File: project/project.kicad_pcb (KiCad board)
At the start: 4 copper layers, 164 x 254 mm, 174 parts

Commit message: adding more things
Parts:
- removed Cs19, Cs20: chair s, -local:chair_small
- removed the R83 at (128.0, 275.0)
- added R12: Painting table, -local:_o_painting_table__, F.Cu at (179.0, 29.0)
- added R20: palet rack2, -local:_o_palet_rack__, F.Cu at (123.0, 115.0)
- added R21: Broken tools, -local:_o_broken_tools_shelf__, F.Cu at (98.5, 58.0)
- added R22: Strings and wheels, -local:_o_strings_wheels_shelf__, F.Cu at (80.0, 68.5)
- added R39: cube container, -local:_o_cube_container__, F.Cu at (93.0, 86.0)
- added R45: Trash el, -local:_o_trash_electronics__, F.Cu at (99.5, 76.0)
- added R55: Dirty small table, -local:_o_dirty_small_table__, F.Cu at (179.2, 145.5)
- added R58: Presentation chairs, -local:_o_chair_box__, F.Cu at (56.0, 206.0)
- added R65: Lightbox, -local:_e_lightbox__, F.Cu at (136.0, 244.0)
- added R80: el center shitty table, -local:_e_shitty_table__, F.Cu at (102.2, 189.5)
- R19: renamed from R35; value palet rack -> palet rack1
- R68: renamed from R78; footprint -local:_e_kitchen_table2__ -> -local:_e_shitty_table__
- R73: renamed from R69; footprint -local:_e_lab_table_x3__ -> -local:_e_lab_table_normal__
- R74: renamed from R70; footprint -local:_e_lab_table_x3__ -> -local:_e_lab_table_tall__
- R75: renamed from R71; footprint -local:_e_lab_table_x3__ -> -local:_e_lab_table_tall__
- R78: renamed from R74; footprint -local:_e_center_table2__ -> -local:_e_center_table1__
- R99: renamed from R90; footprint -local:_o_rack__ -> -local:_e_rack__
- moved R19 38.1 mm to (123.0, 86.0)
- moved R31 10.7 mm to (144.2, 114.3)
- moved Be7 10.0 mm to (128.8, 231.5)
- moved R99 9.62 mm to (79.5, 186.0), turned to 90 degrees
- moved R53 3.61 mm to (161.0, 143.0)
- moved R54 3.61 mm to (179.0, 142.7)
- moved R57 3.00 mm to (80.0, 226.0)
- moved Cb17 2.83 mm to (178.0, 199.0)
- moved Cb18 2.24 mm to (92.0, 211.0)
- moved Cb3 2.00 mm to (178.0, 209.0)
- moved R72 1.75 mm to (97.8, 235.0)
- moved R7 1.25 mm to (117.8, 25.5)
- moved R6 1.12 mm to (139.0, 55.0)
- renumbered R12 to R13, R13 to R14, R14 to R17, R36 to R18, R19 to R23, R20 to R24, R21 to R25, R22 to R26, R23 to R27, R24 to R28, R25 to R29, R26 to R30, R27 to R31, R28 to R32, R29 to R33, R30 to R34, R31 to R35, R32 to R36, R33 to R37, R34 to R38, R37 to R40, R38 to R41, R39 to R42, R40 to R43, R41 to R44, R42 to R46, R43 to R47, R44 to R48, R45 to R49, R46 to R50, R47 to R51, R48 to R52, R18 to R53, R17 to R54, R49 to R56, R50 to R57, R51 to R59, R52 to R60, R53 to R61, R54 to R62, R55 to R63, R56 to R64, R76 to R66, R77 to R67, R79 to R69, R80 to R70, R81 to R71, R82 to R72, R72 to R76, R73 to R77, R75 to R79, R57 to R81, R58 to R82, R59 to R83, R60 to R84, R61 to R85, R62 to R86, R63 to R87, R64 to R88, R65 to R89, R66 to R90, R67 to R91, R68 to R92, R84 to R93, R85 to R94, R86 to R95, R87 to R96, R88 to R97, R89 to R98
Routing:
- net (no net): track 682.5 -> 683.3 mm

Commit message: moving things around
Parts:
- removed Be8: bench, -local:_e_bench__
- removed the R34 at (164.5, 173.6)
- removed the R38 at (185.5, 173.6)
- removed the R64 at (103.0, 178.0)
- removed the R92 at (203.0, 227.8)
- added R33: clamps, -local:_o_clamps__, F.Cu at (150.0, 116.5)
- added R35: cube container, -local:_o_cube_container_x2__, F.Cu at (107.0, 87.0)
- added R39: palet rack, -local:_o_palet_rack_x4__, F.Cu at (106.5, 58.0)
- added R40: palet rack, -local:_o_palet_rack_x4__, F.Cu at (159.5, 86.0)
- added R44: shitty table, -local:_o_shitty_table_x4__, F.Cu at (203.2, 72.5)
- added R47: trash bucket, -local:_o_trash_bucket_x2__, F.Cu at (188.0, 174.0)
- added R5: cnc router, -local:_o_cnc_mill__, F.Cu at (136.5, 47.5)
- Be1, Be2, Be3, Be4, Be5, Be6, Be7: footprint -local:_e_bench__ -> -local:_e_bench_x7__
- R14: renamed from R13; footprint -local:_o_thin_shelf__ -> -local:_o_thin_shelf_single__
- R19: renamed from R23; footprint -local:_o_wheel_tower2__ -> -local:_o_wheel_tower2_x7__
- R29: renamed from R33; footprint -local:_o_thin_shelf__ -> -local:_o_thin_shelf_x2__
- R3: footprint -local:_o_wheel_tower2__ -> -local:_o_wheel_tower2_x7__
- R30: renamed from R35; footprint -local:_o_thin_shelf__ -> -local:_o_thin_shelf_x2__
- R31: renamed from R37; value ppe -> ppe and files
- R32: renamed from R36; footprint -local:_o_thin_shelf__ -> -local:_o_thin_shelf_single__
- R34: renamed from R39; footprint -local:_o_cube_container__ -> -local:_o_cube_container_x2__
- R37: renamed from R19; value palet rack1 -> palet rack; footprint -local:_o_palet_rack__ -> -local:_o_palet_rack_x4__
- R38: renamed from R20; value palet rack2 -> palet rack; footprint -local:_o_palet_rack__ -> -local:_o_palet_rack_x4__
- R43: value trash bottles -> shitty table; footprint -local:_o_trash_bottles__ -> -local:_o_shitty_table_x4__
- R46: renamed from R41; footprint -local:_o_trash_bucket__ -> -local:_o_trash_bucket_x2__
- R51: renamed from R46; footprint -local:_o_wheel_tower1__ -> -local:_o_wheel_tower1_x7__
- R52: renamed from R47; footprint -local:_o_wheel_tower1__ -> -local:_o_wheel_tower1_x7__
- R53: renamed from R48; footprint -local:_o_wheel_tower1__ -> -local:_o_wheel_tower1_x7__
- R54: renamed from R49; footprint -local:_o_wheel_tower1__ -> -local:_o_wheel_tower1_x7__
- R55: renamed from R50; footprint -local:_o_wheel_tower1__ -> -local:_o_wheel_tower1_x7__
- R56: renamed from R51; footprint -local:_o_wheel_tower1__ -> -local:_o_wheel_tower1_x7__
- R57: renamed from R52; footprint -local:_o_wheel_tower1__ -> -local:_o_wheel_tower1_x7__
- R72: renamed from R68; footprint -local:_e_shitty_table__ -> -local:_o_shitty_table_x4__
- R78: renamed from R74; footprint -local:_e_lab_table_tall__ -> -local:_e_lab_table_tall_x2__
- R79: renamed from R75; footprint -local:_e_lab_table_tall__ -> -local:_e_lab_table_tall_x2__
- R80: renamed from R76; footprint -local:_e_center_table1__ -> -local:_e_center_table1_x3__
- R81: renamed from R77; footprint -local:_e_center_table1__ -> -local:_e_center_table1_x3__
- R82: renamed from R78; footprint -local:_e_center_table1__ -> -local:_e_center_table1_x3__
- R84: renamed from R80; footprint -local:_e_shitty_table__ -> -local:_o_shitty_table_x4__
- R85: renamed from R81; footprint -local:_o_wheel_tower2__ -> -local:_o_wheel_tower2_x7__
- R86: renamed from R82; footprint -local:_o_wheel_tower2__ -> -local:_o_wheel_tower2_x7__
- R87: renamed from R83; footprint -local:_o_wheel_tower2__ -> -local:_o_wheel_tower2_x7__
- R88: renamed from R84; footprint -local:_o_wheel_tower2__ -> -local:_o_wheel_tower2_x7__
- R89: renamed from R85; footprint -local:_o_wheel_tower2__ -> -local:_o_wheel_tower2_x7__
- R90: renamed from R86; footprint -local:_o_wheel_tower2__ -> -local:_o_wheel_tower2_x7__
- R91: renamed from R87; value el1 t -> el; footprint -local:_o_wheel_tower3__ -> -local:_o_wheel_tower3_x5__
- R92: renamed from R88; value el2 t -> el; footprint -local:_o_wheel_tower3__ -> -local:_o_wheel_tower3_x5__
- R93: renamed from R89; value el3 t -> el; footprint -local:_o_wheel_tower3__ -> -local:_o_wheel_tower3_x5__
- R94: renamed from R90; value el4 t -> el; footprint -local:_o_wheel_tower3__ -> -local:_o_wheel_tower3_x5__
- R95: renamed from R91; value el5 t -> el; footprint -local:_o_wheel_tower3__ -> -local:_o_wheel_tower3_x5__
- moved R43 239.7 mm to (106.5, 55.2), turned to 180 degrees
- moved R46 118.8 mm to (80.0, 130.0), turned to 90 degrees
- moved R50 97.8 mm to (107.0, 173.5), turned to 180 degrees
- moved R49 93.3 mm to (203.0, 118.0), turned to -90 degrees
- moved R90 81.1 mm to (203.0, 228.8), turned to -90 degrees
- moved R48 68.0 mm to (187.0, 117.0), turned to -90 degrees
- moved R28 65.8 mm to (203.2, 101.8), turned to -90 degrees
- moved R84 62.3 mm to (143.5, 142.8), turned to 0 degrees
- moved R24 60.2 mm to (124.0, 115.5), turned to 0 degrees
- moved R76 58.4 mm to (93.2, 176.8), turned to 0 degrees
- moved R23 57.0 mm to (150.2, 57.8), turned to 0 degrees
- moved R60 56.8 mm to (122.5, 143.2), turned to 0 degrees
- moved R8 55.1 mm to (164.2, 55.0), turned to 180 degrees
- moved R59 53.1 mm to (183.0, 89.8)
- moved R17 43.7 mm to (180.5, 142.5), turned to 180 degrees
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- renumbered R9 to R10, R97 to R100, R98 to R101, R99 to R102, R10 to R11, R11 to R12, R12 to R13, R14 to R15, R15 to R16, R16 to R17, R17 to R18, R24 to R20, R25 to R21, R26 to R22, R27 to R23, R28 to R24, R29 to R25, R30 to R26, R31 to R27, R32 to R28, R18 to R36, R21 to R41, R22 to R42, R40 to R45, R42 to R48, R44 to R49, R45 to R50, R53 to R58, R54 to R59, R5 to R6, R55 to R60, R56 to R61, R57 to R62, R58 to R63, R59 to R64, R60 to R65, R61 to R66, R62 to R67, R63 to R68, R65 to R69, R6 to R7, R66 to R70, R67 to R71, R69 to R73, R70 to R74, R71 to R75, R72 to R76, R73 to R77, R7 to R8, R79 to R83, R8 to R9, R93 to R96, R94 to R97, R95 to R98, R96 to R99
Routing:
- net Net-(L1-Pad1): track 1827.7 -> 1941.7 mm
- net (no net): track 683.3 -> 716.4 mm
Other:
- copper layers 4 -> 6
- board text added: "needs: * 1f 4A"
- board text added: "needs: * 3f 4A"

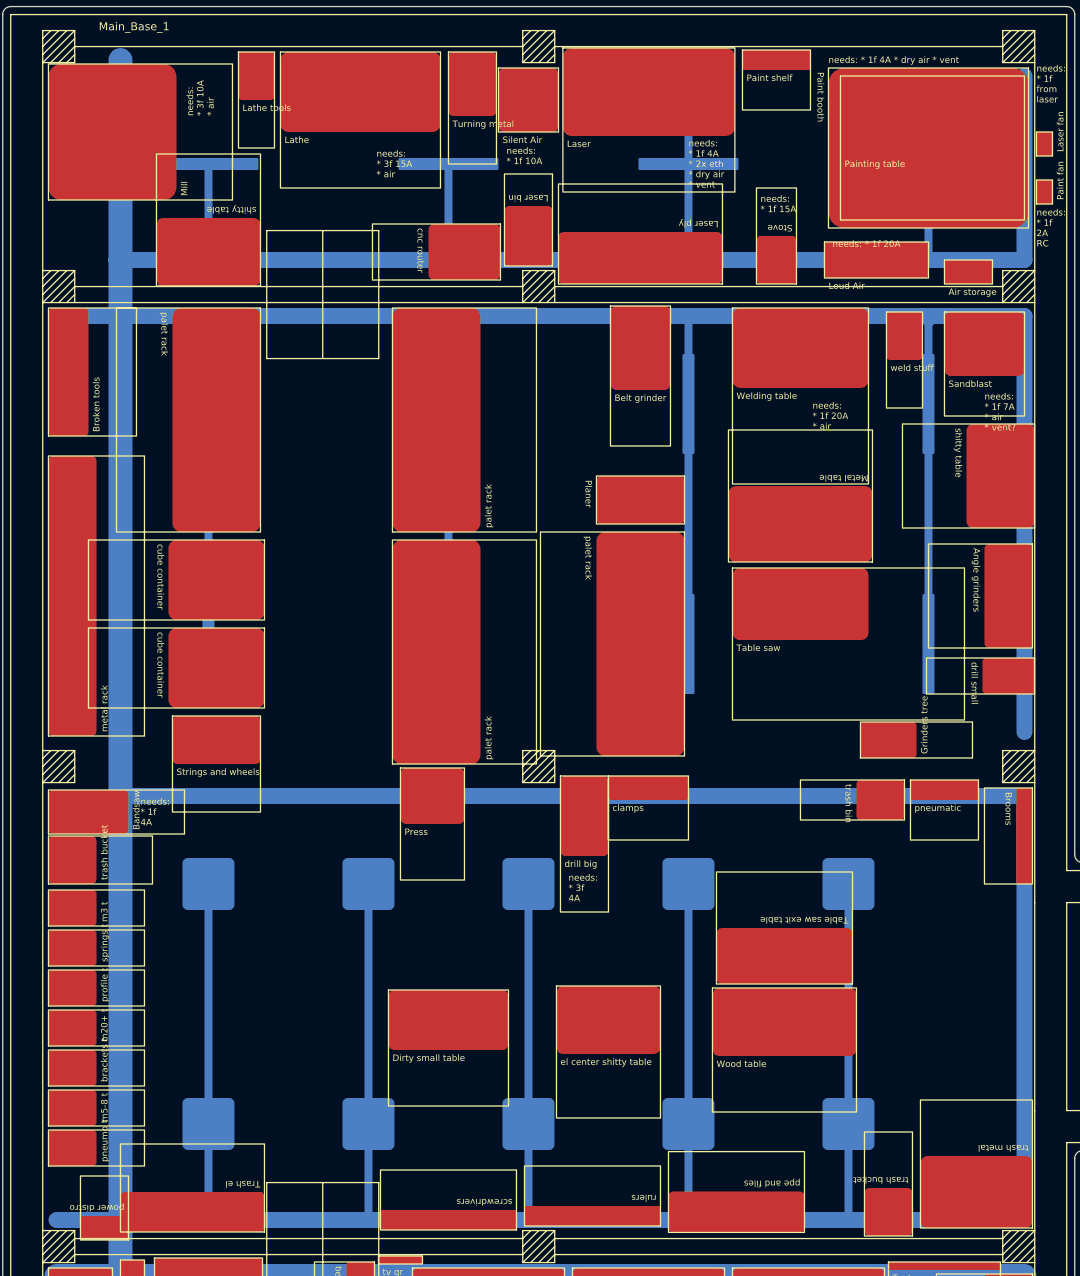
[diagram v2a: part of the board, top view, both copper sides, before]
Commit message: adding light and moving electrical stuff
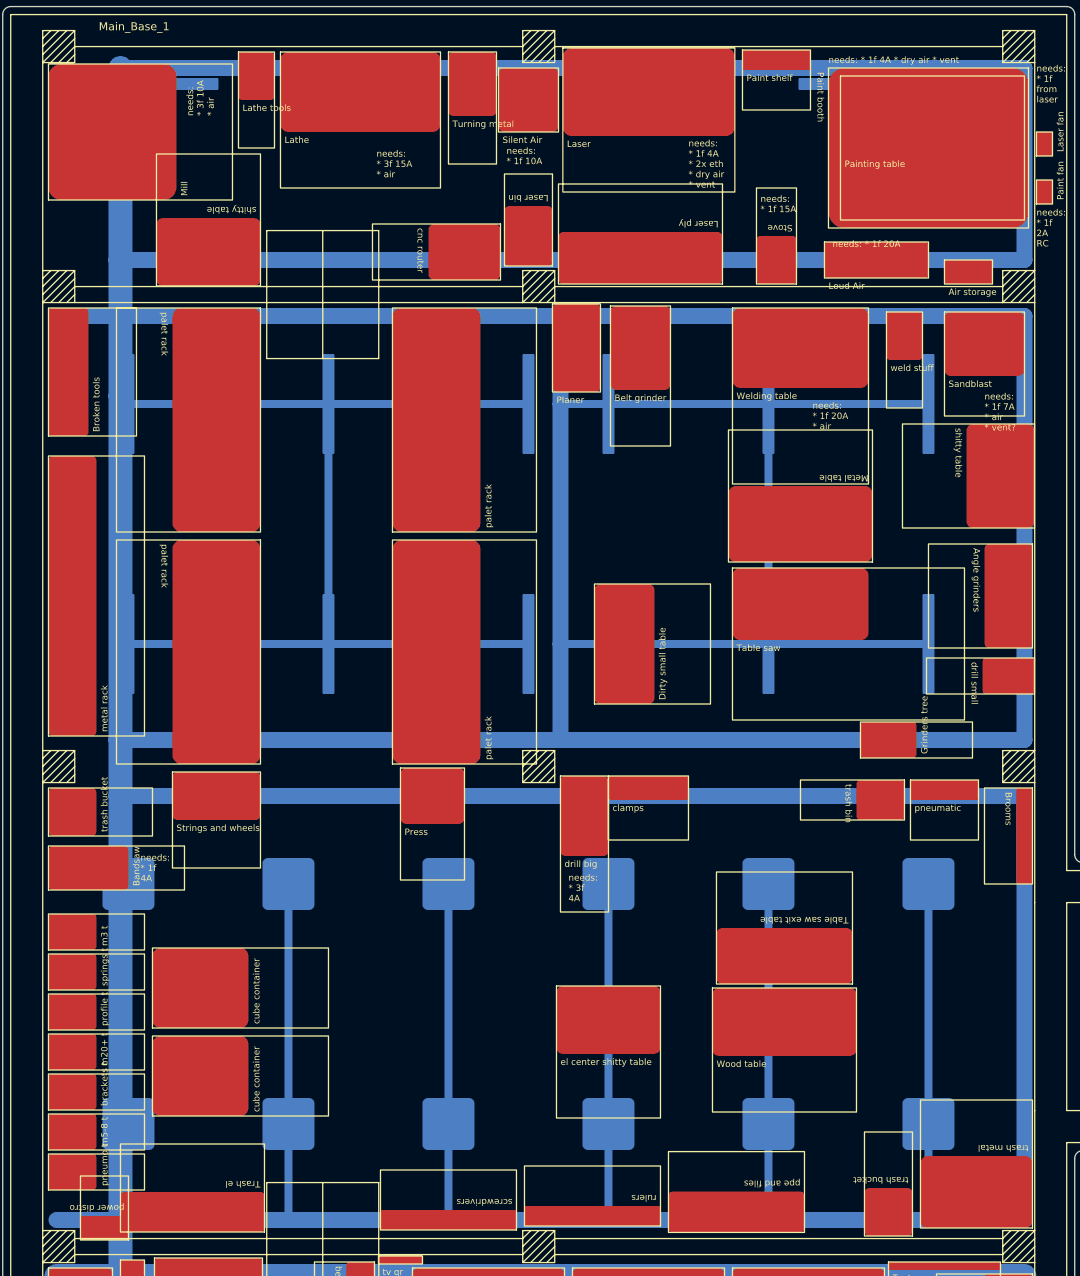
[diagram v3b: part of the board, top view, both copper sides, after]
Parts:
- removed the L31 at (160.0, 100.0)
- removed the L32 at (190.0, 70.0)
- added L24: light, -local:light_square, B.Cu at (130.0, 160.0)
- added L25: light, -local:light_square, B.Cu at (130.0, 130.0)
- added L34: light, -local:light_long, B.Cu at (190.0, 70.0)
- added L35: light, -local:light_long, B.Cu at (155.0, 30.0)
- added L38: light, -local:light_long, B.Cu at (180.0, 30.0)
- added L39: light, -local:light_long, B.Cu at (170.0, 100.0)
- added L40: light, -local:light_long, B.Cu at (175.0, 60.0)
- added L41: light, -local:light_long, B.Cu at (150.0, 70.0)
- added L42: light, -local:light_long, B.Cu at (150.0, 100.0)
- added L43: light, -local:light_long, B.Cu at (170.0, 70.0)
- moved L33 63.2 mm to (140.0, 100.0), turned to -90 degrees
- moved R34 62.6 mm to (93.0, 159.0), turned to 90 degrees
- moved R35 62.6 mm to (93.0, 148.0), turned to 90 degrees
- moved R40 53.0 mm to (106.5, 87.0)
- moved R60 44.1 mm to (148.2, 107.5), turned to 90 degrees
- moved R25 27.1 mm to (143.0, 57.5), turned to 0 degrees
- moved L29 20.0 mm to (140.0, 70.0)
- moved L27 15.0 mm to (115.0, 100.0)
- moved L30 15.0 mm to (115.0, 70.0)
- moved L32 14.1 mm to (120.0, 30.0)
- moved L26 11.2 mm to (195.0, 30.0)
- moved L37 11.2 mm to (95.0, 30.0)
- moved L12 10.0 mm to (90.0, 130.0)
- moved L13 10.0 mm to (110.0, 130.0)
- moved L14 10.0 mm to (110.0, 160.0)
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- renumbered L24 to L26, L25 to L27, L26 to L28, L27 to L29, L28 to L30, L29 to L31, L30 to L32, L34 to L36, L35 to L37
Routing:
- net Net-(L1-Pad1): track 1941.7 -> 2248.7 mm

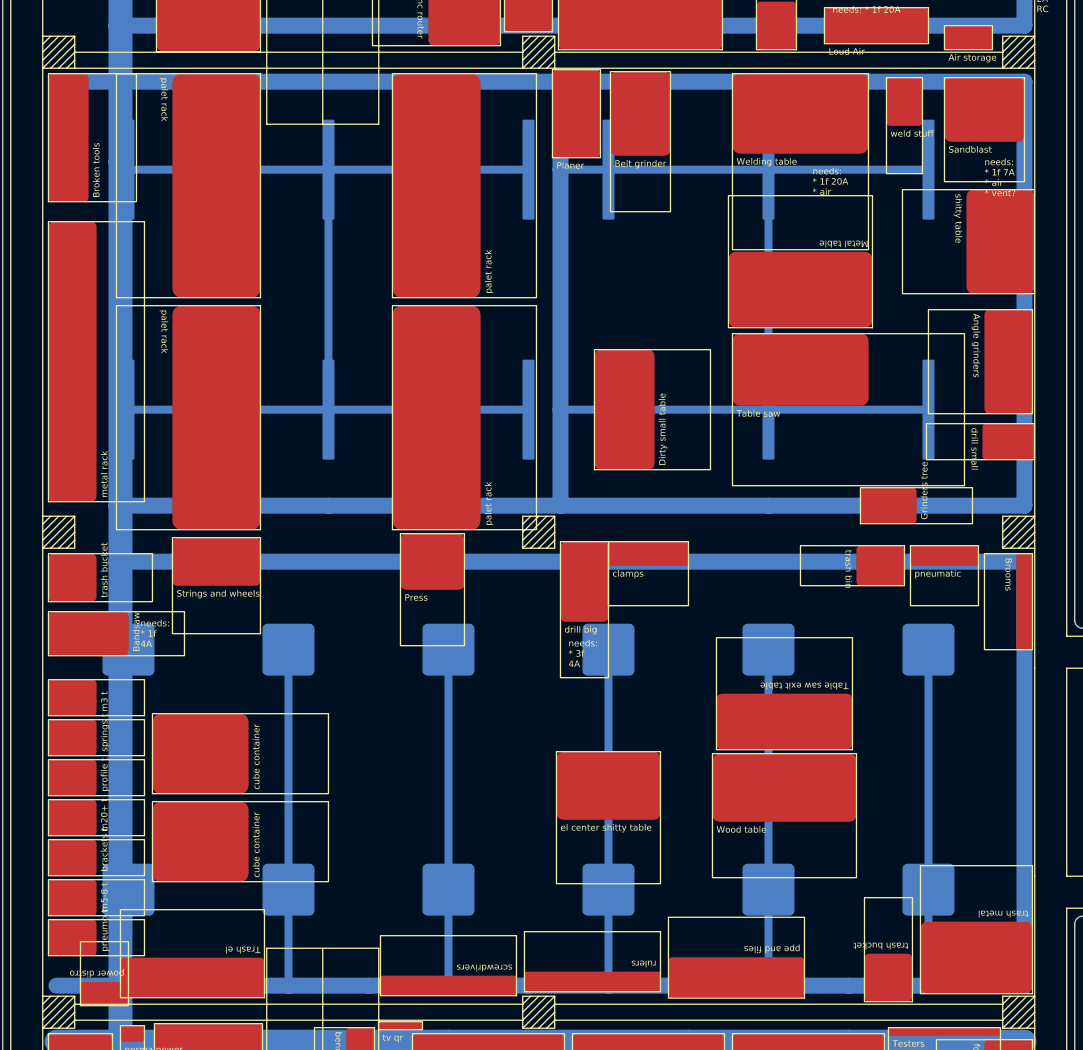
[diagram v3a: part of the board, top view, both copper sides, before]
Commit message: reworking dirty workshop
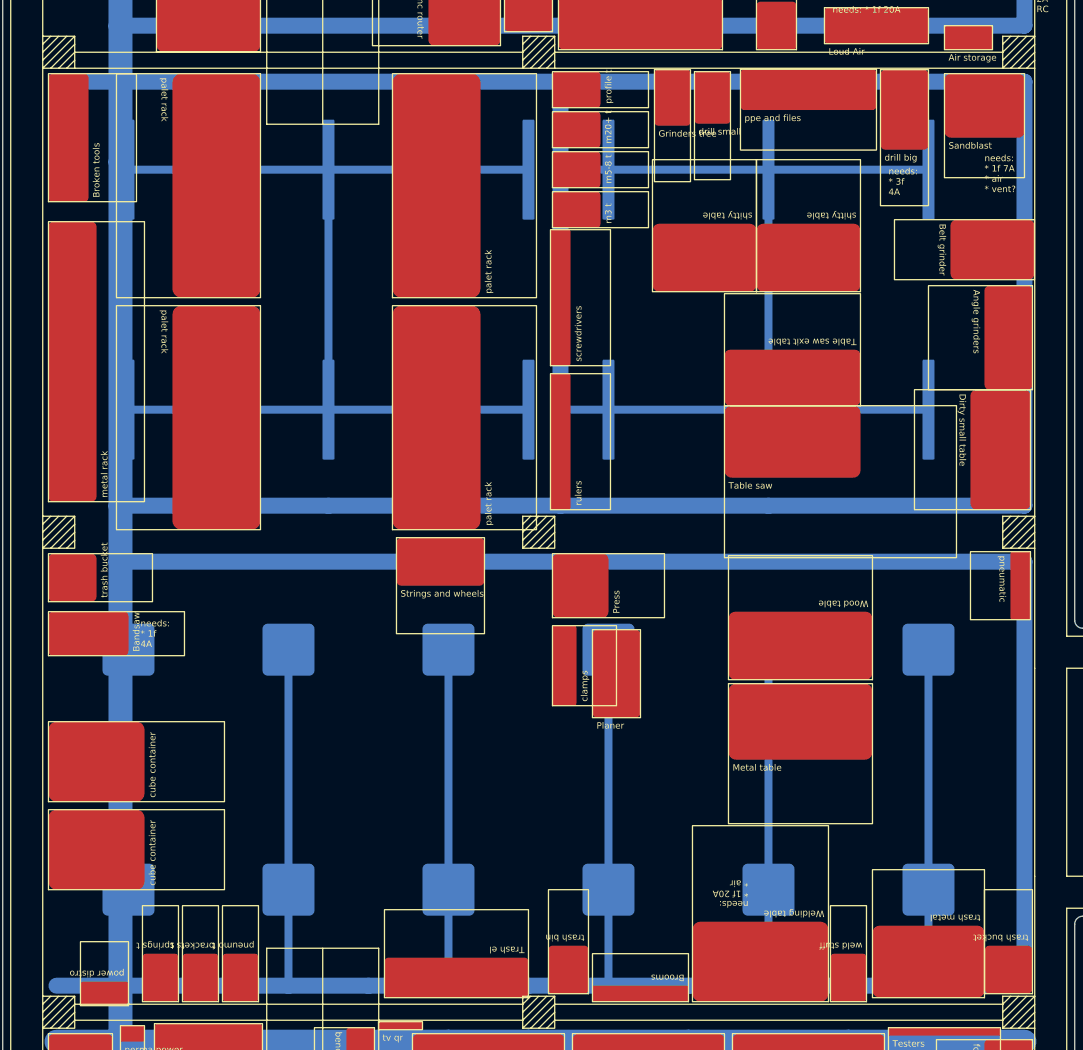
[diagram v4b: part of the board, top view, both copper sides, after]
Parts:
- R84: value el center shitty table -> shitty table
- moved R18 116.6 mm to (177.5, 174.0), turned to 180 degrees
- moved R31 116.4 mm to (166.5, 57.5), turned to 0 degrees
- moved R19 115.5 mm to (182.2, 174.0), turned to 180 degrees
- moved R56 110.7 mm to (143.0, 72.2)
- moved R53 106.6 mm to (143.0, 67.2)
- moved R57 106.6 mm to (143.0, 62.2)
- moved R54 87.7 mm to (143.0, 77.2)
- moved R29 78.9 mm to (142.8, 94.5), turned to 90 degrees
- moved R27 71.3 mm to (184.0, 57.5)
- moved R49 70.6 mm to (160.0, 174.0), turned to 180 degrees
- moved R25 70.2 mm to (148.0, 127.5)
- moved R48 68.5 mm to (147.5, 173.0), turned to 180 degrees
- moved R84 62.7 mm to (168.5, 85.2), turned to 180 degrees
- moved R22 62.3 mm to (155.8, 57.5), turned to 0 degrees
- moved R30 61.8 mm to (142.8, 112.5), turned to 90 degrees
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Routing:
- net (no net): track 716.4 -> 715.6 mm
